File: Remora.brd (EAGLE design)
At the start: 86.4 x 66.7 mm, 81 parts, among them IC1 MCP23017, J2 GROVE-I2C, P1 PADSMALL, T1 2N3904, T2 BSS138

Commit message: Mise à jour du PCB et ajout d'images
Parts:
- RELAIS: value G3MC-202P -> G3MC-202P-5V
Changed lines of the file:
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@@
 <attribute name="OC_FARNELL" value="unknown" x="4.7752" y="18.6182" size="1.778" layer="27" rot="R270" display="off"/>
 </element>
-<element name="RELAIS" library="sip-4" package="SIP-4" value="G3MC-202P" x="26.67" y="12.7" rot="R90"/>
+<element name="RELAIS" library="sip-4" package="SIP-4" value="G3MC-202P-5V" x="26.67" y="12.7" smashed="yes" rot="R90">
+<attribute name="NAME" x="19.3" y="11.99" size="1.778" layer="25" rot="R90"/>
+<attribute name="VALUE" x="23.05" y="7.81" size="1.778" layer="27" rot="R90"/>
+</element>
 </elements>
 <signals>

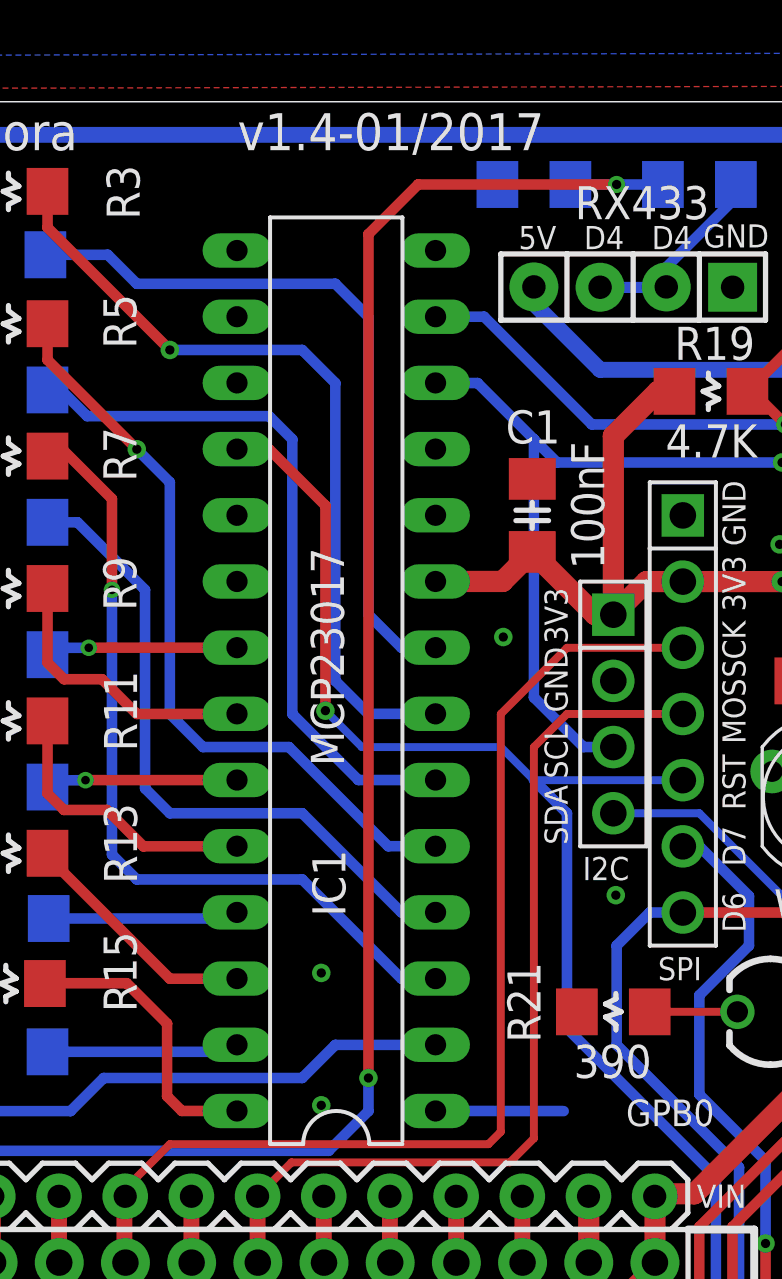
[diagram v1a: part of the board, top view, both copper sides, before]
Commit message: Correction d'une anomalie de connexion de la LED rouge
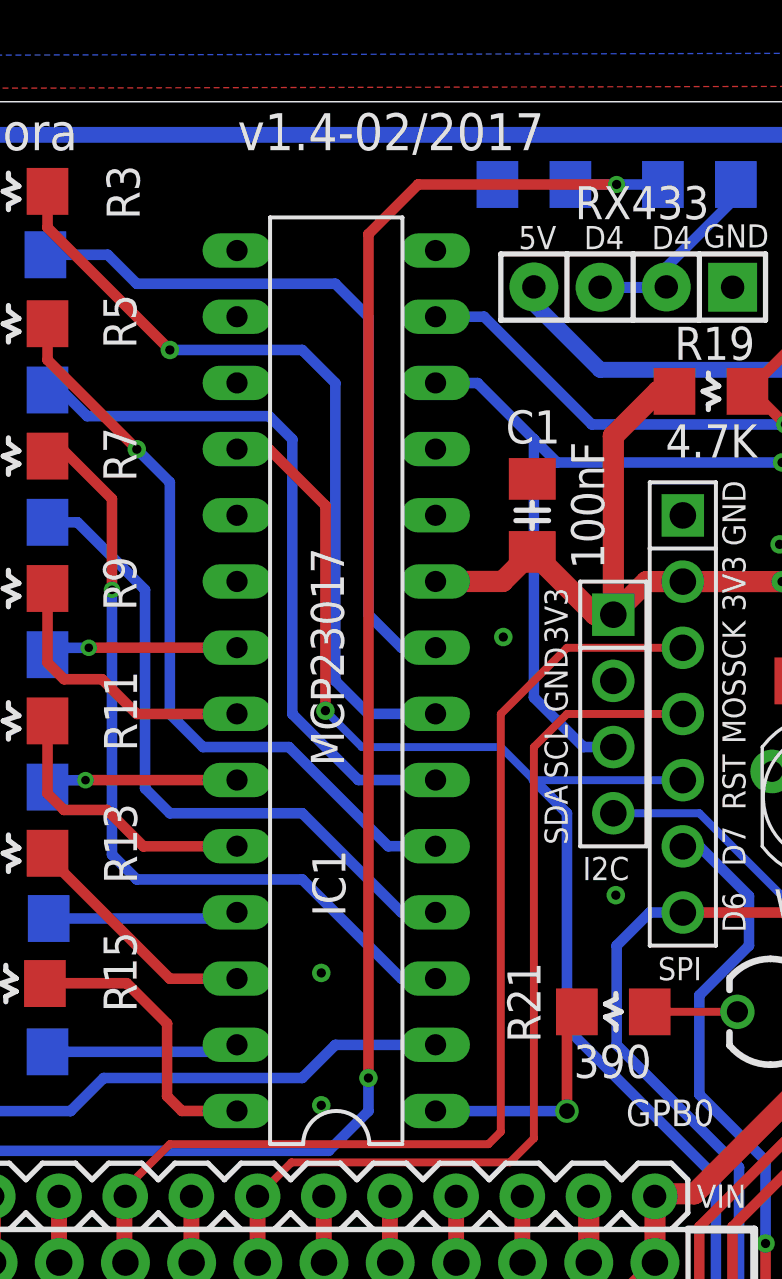
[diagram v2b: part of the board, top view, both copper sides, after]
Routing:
- net LED: track 5.37 -> 9.24 mm, vias 0 -> 2
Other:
- board text added: "v1.4-02/2017"
- board text removed: "v1.4-01/2017"
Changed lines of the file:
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@@
 <text x="72.14125" y="59.9775" size="0.889" layer="26" font="vector" ratio="15" rot="MR270">SDA</text>
 <text x="38.862" y="9.5885" size="1.397" layer="25" font="vector" ratio="15">Spark Core / Photon</text>
-<text x="51.66079375" y="65.52568125" size="1.4224" layer="21" font="vector" ratio="15" align="center">v1.4-01/2017</text>
+<text x="51.66079375" y="65.52568125" size="1.4224" layer="21" font="vector" ratio="15" align="center">v1.4-02/2017</text>
 <wire x1="2.54" y1="0" x2="80.645" y2="0" width="0.0254" layer="20"/>
 <wire x1="80.645" y1="0" x2="86.36" y2="5.715" width="0.0254" layer="20"/>
@@
 <signal name="LED">
 <contactref element="IC1" pad="1"/>
-<wire x1="53.3755625" y1="27.945078125" x2="54.615078125" y2="27.945078125" width="0.4064" layer="16"/>
-<wire x1="54.615078125" y1="27.945078125" x2="58.293" y2="27.94" width="0.4064" layer="16"/>
 <contactref element="R21" pad="1"/>
-<wire x1="59.1185" y1="31.4295" x2="58.798" y2="31.75" width="0.3048" layer="1"/>
-<wire x1="58.293" y1="27.94" x2="59.1185" y2="31.4295" width="0" layer="19" extent="1-16"/>
+<wire x1="58.798" y1="31.75" x2="58.42" y2="31.75" width="0.4064" layer="1"/>
+<wire x1="58.42" y1="31.75" x2="58.42" y2="27.94" width="0.4064" layer="1"/>
+<wire x1="58.42" y1="27.94" x2="53.3755625" y2="27.94" width="0.4064" layer="16"/>
+<wire x1="53.3755625" y1="27.94" x2="53.3755625" y2="27.945078125" width="0.4064" layer="1"/>
+<via x="58.42" y="27.94" extent="1-16" drill="0.6" shape="square"/>
+<via x="53.3755625" y="27.94" extent="1-16" drill="0.6" shape="square"/>
 </signal>
 <signal name="N$17">

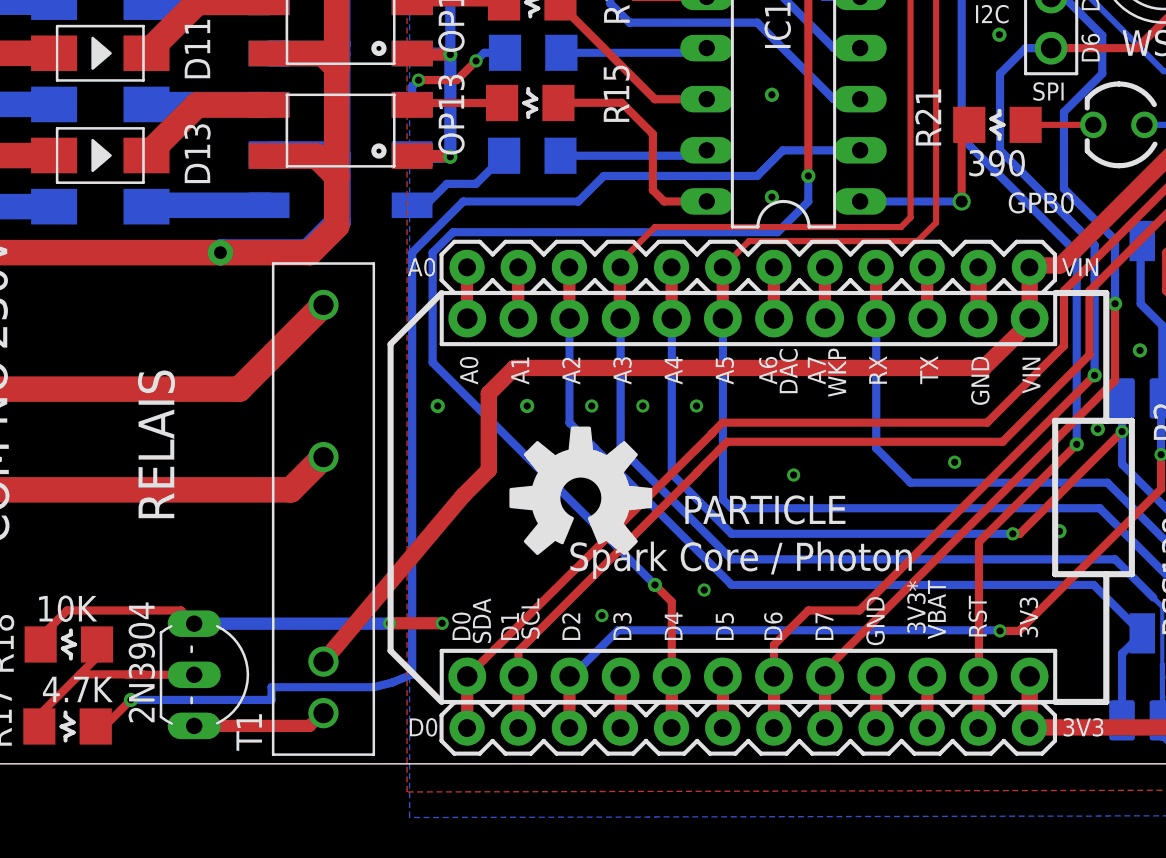
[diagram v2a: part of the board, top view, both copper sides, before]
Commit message: Correction d'anomalie sur la route de la LED
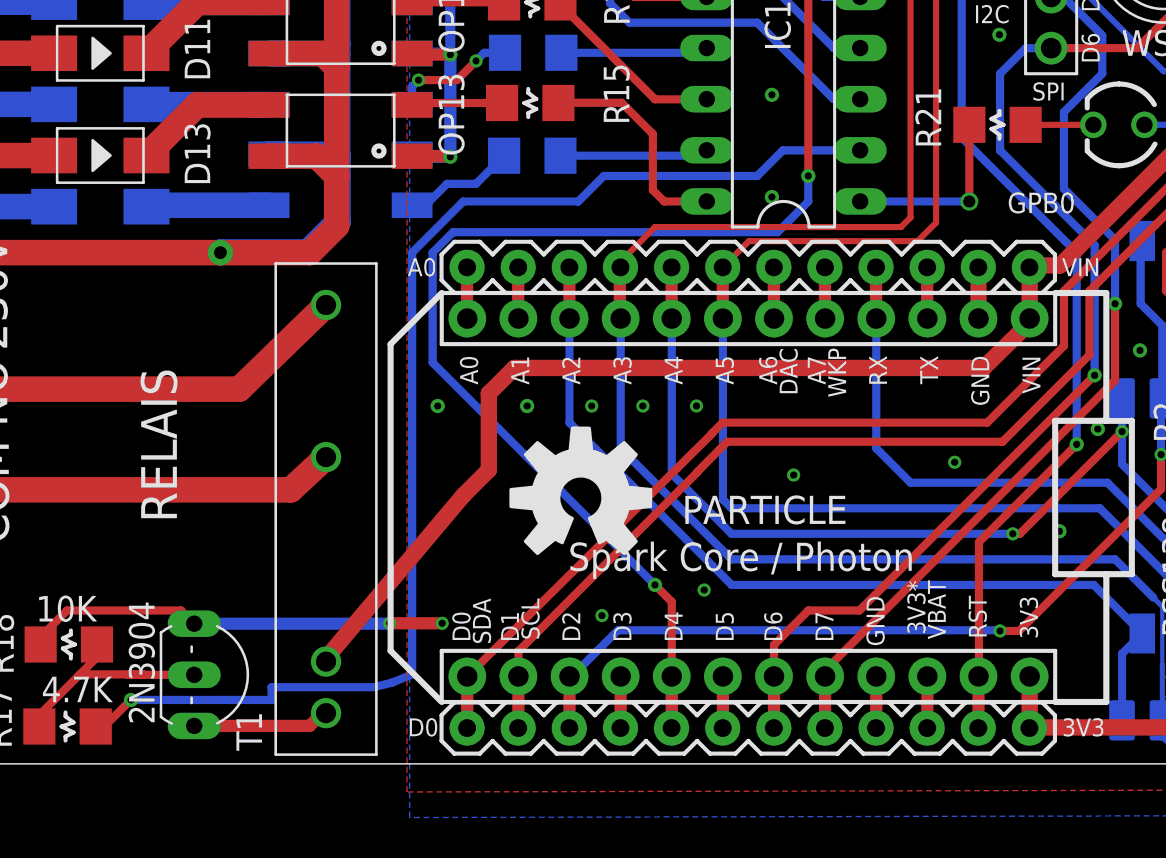
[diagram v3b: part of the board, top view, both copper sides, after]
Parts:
- moved RELAIS 0.13 mm to (26.8, 12.7)
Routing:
- net LED: track 9.24 -> 9.61 mm, vias 2 -> 1
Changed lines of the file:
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@@
 <element name="R21" library="_c2h" package="1206-RES" value="390" x="60.198" y="31.75" smashed="yes">
 <attribute name="NAME" x="56.134" y="33.655" size="1.27" layer="25" font="vector" ratio="15" rot="R270"/>
-<attribute name="VALUE" x="58.674" y="29.21" size="1.27" layer="25" font="vector" ratio="15"/>
 </element>
 <element name="LED" library="_c2h" package="LED3MM" value="LED3MM" x="66.2305" y="31.75" smashed="yes" rot="R180">
@@
 <attribute name="OC_FARNELL" value="unknown" x="4.7752" y="18.6182" size="1.778" layer="27" rot="R270" display="off"/>
 </element>
-<element name="RELAIS" library="sip-4" package="SIP-4" value="G3MC-202P-5V" x="26.67" y="12.7" smashed="yes" rot="R90">
-<attribute name="NAME" x="19.3" y="11.99" size="1.778" layer="25" rot="R90"/>
-<attribute name="VALUE" x="23.05" y="7.81" size="1.778" layer="27" rot="R90"/>
+<element name="RELAIS" library="sip-4" package="SIP-4" value="G3MC-202P-5V" x="26.797" y="12.7" smashed="yes" rot="R90">
+<attribute name="NAME" x="19.427" y="11.99" size="1.778" layer="25" rot="R90"/>
+<attribute name="VALUE" x="23.177" y="7.81" size="1.778" layer="27" rot="R90"/>
 </element>
 </elements>
@@
 <wire x1="72.771" y1="50.038" x2="75.819" y2="46.99" width="0.8128" layer="16"/>
 <contactref element="RELAIS" pad="+(3)"/>
-<wire x1="26.71" y1="5.08" x2="26.7208" y2="5.1054" width="0" layer="19" extent="1-1"/>
+<wire x1="26.837" y1="5.08" x2="26.7208" y2="5.1054" width="0" layer="19" extent="1-1"/>
 </signal>
 <signal name="GND">
@@
 <contactref element="IC1" pad="1"/>
 <contactref element="R21" pad="1"/>
-<wire x1="58.798" y1="31.75" x2="58.42" y2="31.75" width="0.4064" layer="1"/>
-<wire x1="58.42" y1="31.75" x2="58.42" y2="27.94" width="0.4064" layer="1"/>
-<wire x1="58.42" y1="27.94" x2="53.3755625" y2="27.94" width="0.4064" layer="16"/>
-<wire x1="53.3755625" y1="27.94" x2="53.3755625" y2="27.945078125" width="0.4064" layer="1"/>
-<via x="58.42" y="27.94" extent="1-16" drill="0.6" shape="square"/>
-<via x="53.3755625" y="27.94" extent="1-16" drill="0.6" shape="square"/>
+<wire x1="58.798" y1="31.75" x2="58.798" y2="31.4295" width="0" layer="19" extent="1-16"/>
+<wire x1="53.3755625" y1="27.945078125" x2="58.798" y2="27.94" width="0.4064" layer="16"/>
+<wire x1="58.798" y1="27.94" x2="58.42" y2="27.94" width="0.4064" layer="16"/>
+<wire x1="58.798" y1="27.94" x2="58.798" y2="31.75" width="0.4064" layer="1"/>
+<wire x1="58.798" y1="31.4295" x2="58.798" y2="31.75" width="0" layer="19" extent="1-16"/>
+<via x="58.798" y="27.94" extent="1-16" drill="0.6" shape="square"/>
 </signal>
 <signal name="N$17">
@@
 <wire x1="26.014678125" y1="1.884678125" x2="26.67" y2="2.54" width="0.6096" layer="1"/>
 <wire x1="26.67" y1="2.54" x2="26.69" y2="2.54" width="0.4064" layer="1"/>
-<wire x1="26.69" y1="2.54" x2="26.71" y2="2.52" width="0.4064" layer="1"/>
+<wire x1="26.69" y1="2.54" x2="26.837" y2="2.52" width="0.4064" layer="1"/>
 </signal>
 <signal name="NO">
@@
 <contactref element="230V" pad="2"/>
 <wire x1="4.7752" y1="18.6182" x2="22.5282" y2="18.6182" width="1.27" layer="1"/>
-<wire x1="22.5282" y1="18.6182" x2="26.71" y2="22.8" width="1.27" layer="1"/>
+<wire x1="22.5282" y1="18.6182" x2="26.837" y2="22.8" width="1.27" layer="1"/>
 </signal>
 <signal name="COM">
@@
 <contactref element="230V" pad="3"/>
 <wire x1="4.7752" y1="13.6144" x2="25.0844" y2="13.6144" width="1.27" layer="1"/>
-<wire x1="25.0844" y1="13.6144" x2="26.71" y2="15.24" width="1.27" layer="1"/>
+<wire x1="25.0844" y1="13.6144" x2="26.837" y2="15.24" width="1.27" layer="1"/>
 </signal>
 </signals>

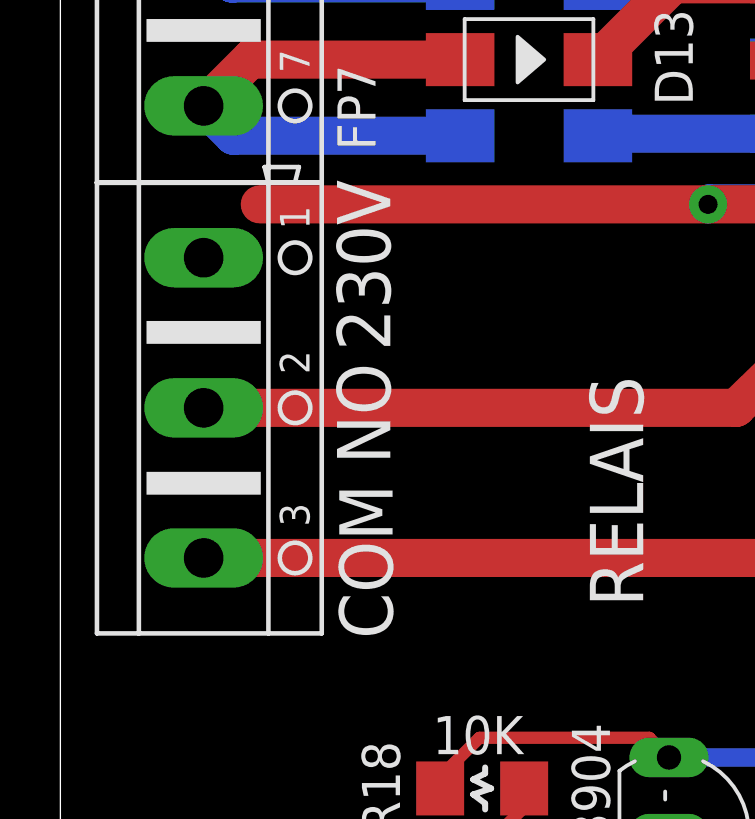
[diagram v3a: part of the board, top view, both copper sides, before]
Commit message: Correction d'anomalie de la route de la phase
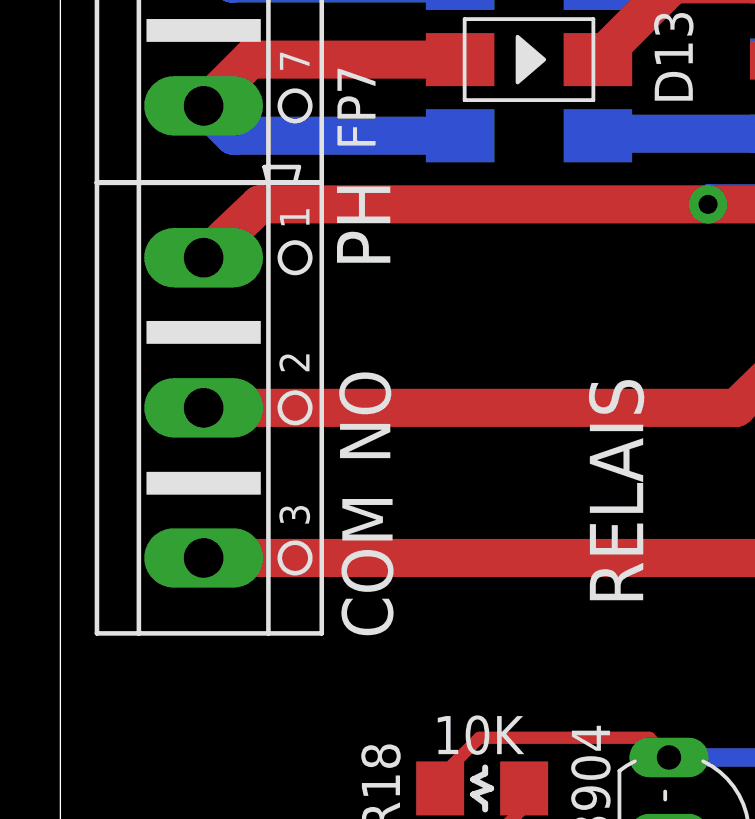
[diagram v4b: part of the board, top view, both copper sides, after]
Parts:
- renumbered 230V to PH
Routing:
- net PHASE: track 145.0 -> 147.5 mm
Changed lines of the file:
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@@
 <text x="73.369" y="56.418" size="1.27" layer="26" font="vector" ratio="15" rot="MR270">5V</text>
 <text x="76.4805" y="57.561" size="1.27" layer="26" font="vector" ratio="15" rot="MR270">3V3</text>
-<text x="10.9982" y="16.7386" size="1.778" layer="25" rot="R90">NO</text>
-<text x="11.0744" y="10.922" size="1.778" layer="25" rot="R90">COM</text>
+<text x="10.9982" y="16.7386" size="1.6764" layer="25" rot="R90">NO</text>
+<text x="11.0744" y="10.922" size="1.6764" layer="25" rot="R90">COM</text>
 </plain>
 <attributes>
@@
 <attribute name="VALUE" x="78.359" y="44.2595" size="1.27" layer="27" rot="R270"/>
 </element>
-<element name="230V" library="con-ptr500" package="AK500/3" value="" x="4.7752" y="18.6182" rot="R270">
+<element name="PH" library="con-ptr500" package="AK500/3" value="" x="4.7752" y="18.6182" rot="R270">
 <attribute name="OC_NEWARK" value="unknown" x="4.7752" y="18.6182" size="1.778" layer="27" rot="R270" display="off"/>
 <attribute name="MPN" value="" x="4.7752" y="18.6182" size="1.778" layer="27" rot="R270" display="off"/>
@@
 <wire x1="26.9985" y1="55.615" x2="27.3685" y2="55.245" width="1.27" layer="1"/>
 <wire x1="26.035" y1="25.4" x2="21.59" y2="25.4" width="1.27" layer="1"/>
-<contactref element="230V" pad="1"/>
-<wire x1="4.7752" y1="23.622" x2="6.6464" y2="25.4" width="0" layer="19" extent="1-1"/>
+<contactref element="PH" pad="1"/>
+<wire x1="6.6464" y1="25.4" x2="4.7752" y2="23.622" width="1.27" layer="1"/>
 </signal>
 <signal name="+5V">
@@
 <signal name="NO">
 <contactref element="RELAIS" pad="1"/>
-<contactref element="230V" pad="2"/>
+<contactref element="PH" pad="2"/>
 <wire x1="4.7752" y1="18.6182" x2="22.5282" y2="18.6182" width="1.27" layer="1"/>
 <wire x1="22.5282" y1="18.6182" x2="26.837" y2="22.8" width="1.27" layer="1"/>
@@
 <signal name="COM">
 <contactref element="RELAIS" pad="2"/>
-<contactref element="230V" pad="3"/>
+<contactref element="PH" pad="3"/>
 <wire x1="4.7752" y1="13.6144" x2="25.0844" y2="13.6144" width="1.27" layer="1"/>
 <wire x1="25.0844" y1="13.6144" x2="26.837" y2="15.24" width="1.27" layer="1"/>
